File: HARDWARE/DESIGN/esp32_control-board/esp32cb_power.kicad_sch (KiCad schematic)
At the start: 26 parts, among them J301 ESP32m_Prog, U2 LM63615DQDRRRQ1, U3 H7651-33PR, U302 USBLC6-2SC6, U4 AMS1117-3.3

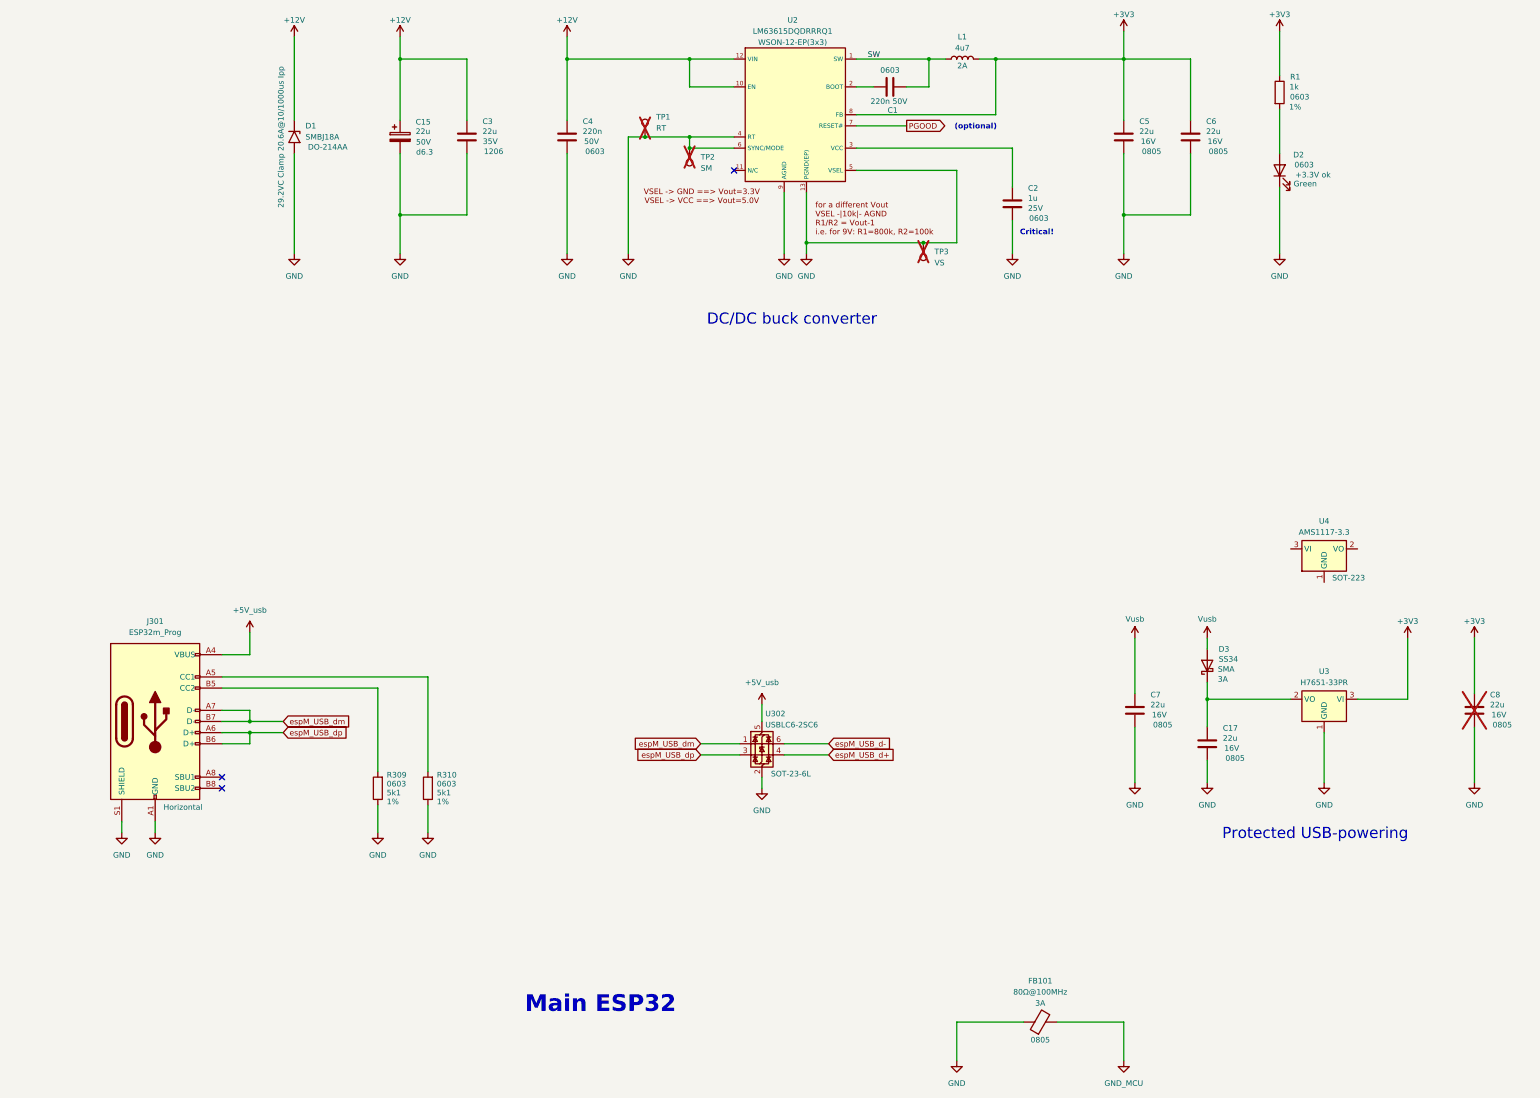
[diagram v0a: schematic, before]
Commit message: 60707 - schematics and readme updated, preliminary PCB-layout prepared
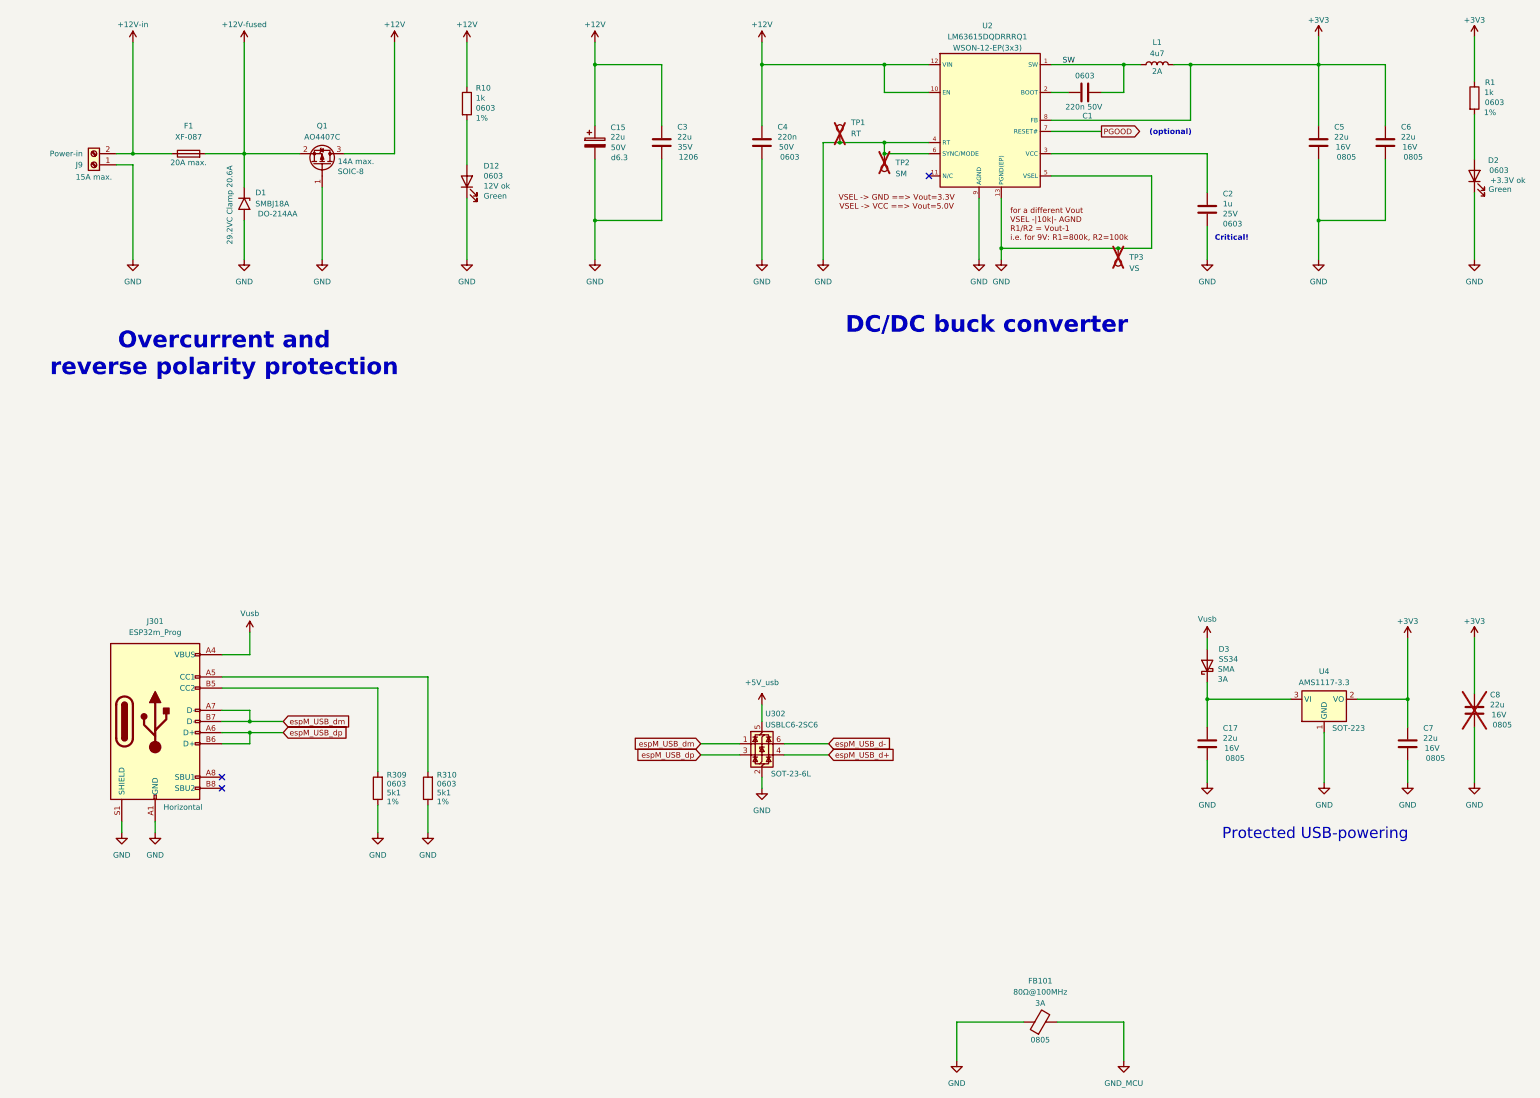
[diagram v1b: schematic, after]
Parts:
- removed U3: H7651-33PR, Package_TO_SOT_SMD:SOT-89-3, symbol Regulator_Linear:AMS1117-3.3
- added D12: 12V ok, LED_SMD:LED_0603_1608Metric, symbol Device:LED
- added F1: XF-087, Fuse:FuseHolder_Blade_ATO_Littelfuse_FLR_178.6165, symbol Device:Fuse
- added J9: Power-in, Connector_AMASS:AMASS_XT30PW-M_1x02_P2.50mm_Horizontal, symbol Connector:Screw_Terminal_01x02
- added Q1: AO4407C, (FOOTPRINTS):SOIC-8_P-MOSFET, symbol Transistor_FET:AO3401A
- added R10: 1k, Resistor_SMD:R_0603_1608Metric, symbol Device:R
- D1: LCSC (none) -> C151256; LCSC part C151256 -> (none); Property 29.2VC Clamp 20.6A@10/1000us Ipp -> 29.2VC Clamp 20.6A
- J301: footprint NICKO:C3151749_USB_TYPE-C_Vertical -> (FOOTPRINTS):C3151749_USB_TYPE-C_Vertical
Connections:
- net +12V: now also Q1.3 (D), R10.1; no longer D1.1 (A1)
- net +3V3: now also C7.1, U4.2 (VO)
- net +5V_usb: no longer J301.A4 (VBUS), J301.A9 (VBUS), J301.B4 (VBUS), J301.B9 (VBUS)
- net GND: now also U4.1 (GND), D12.1 (K), J9.1 (Pin_1), Q1.1 (G)
- net Vusb: now also J301.A4 (VBUS), J301.A9 (VBUS), J301.B4 (VBUS), J301.B9 (VBUS); no longer C7.1
- net at C17.1, D3.1 (K): now also U4.3 (VI)
- new net: D12.2 (A), R10.2
- new net +12V-fused: D1.1 (A1), F1.2, Q1.2 (S)
- new net +12V-in: F1.1, J9.2 (Pin_2)
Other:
- note added: "Overcurrent and reverse polarity protection"
- note removed: "Main ESP32"
- title: (none) -> ESP32-based Control Board
- moved on the sheet: C1, C15, C2, C3, C4, C5, C6, C7, D1, D2, L1, R1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

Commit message: 60710 - schematic and PCB-layout updated
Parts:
- removed J301: ESP32m_Prog, (FOOTPRINTS):C3151749_USB_TYPE-C_Vertical, symbol Connector:USB_C_Receptacle_USB2.0
- removed R10: 1k, Resistor_SMD:R_0603_1608Metric, symbol Device:R
- removed R309, R310: 5k1, Resistor_SMD:R_0603_1608Metric, symbol Device:R
- removed U302: USBLC6-2SC6, Package_TO_SOT_SMD:SOT-23-6, symbol Power_Protection:USBLC6-2SC6
- added C322, C323: 100n, Capacitor_SMD:C_0603_1608Metric, symbol Device:C
- added D14: MMSZ5242B, Diode_SMD:D_SOD-123, symbol Diode:BZX84Cxx
- added Q3: DMP3013SFV-7, Package_SON:Diodes_PowerDI3333-8, symbol Transistor_FET:DMP3013SFV
- added R340: 12k, Resistor_SMD:R_0603_1608Metric, symbol Device:R
- added R343: 5k1, Resistor_SMD:R_0603_1608Metric, symbol Device:R
- Q1: now not fitted; now left out of the parts list
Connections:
- net +12V: now also C322.2, D14.1 (K), Q3.1 (S), Q3.2 (S), Q3.3 (S), R343.2; no longer Q1.3 (D)
- net +12V-fused: now also C323.2, Q3.5 (D); no longer Q1.2 (S)
- net GND: now also C323.1, R340.2; no longer Q1.1 (G)
- net at D12.2 (A): now also R343.1
- new net: C322.1, D14.2 (A), Q3.4 (G), R340.1
- no-connect marks 3 -> 1
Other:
- note added: "Overcurrent and overvoltage protection"
- note added: "Reverse polarity protection"
- note added: "USB-line reverse-current protection"
- note removed: "Overcurrent and reverse polarity protection"
- note removed: "Protected USB-powering"
- moved on the sheet: C1, C15, C17, C2, C3, C4, C5, C6, C7, C8, D1, D12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

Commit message: 60714 - one of two I2C-mux ICs was removed, PCB-layout finished, start tracing
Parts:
- renumbered C15 to C101, C3 to C102, C4 to C103, C323 to C104, C1 to C105, C2 to C106, C322 to C107, C5 to C108, C6 to C109, C17 to C110, C7 to C111, C8 to C112, D1 to D101, D14 to D102, D12 to D103, D2 to D104, D3 to D105, F1 to F101, J9 to J101, L1 to L101, Q1 to Q101, Q3 to Q102, R340 to R101, R343 to R102, R1 to R103, TP1 to TP101, TP2 to TP102, TP3 to TP103, U2 to U101, U4 to U102
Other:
- moved on the sheet: C107, Q101

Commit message: 60825 - Schematic update and PCB-layout started
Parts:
- removed FB101: 80Ω@100MHz, Inductor_SMD:L_0805_2012Metric, symbol Device:FerriteBead
- removed R101: 12k, Resistor_SMD:R_0603_1608Metric, symbol Device:R
- added R108: 12k, Resistor_SMD:R_0603_1608Metric, symbol Device:R
- added R215: 0R, Resistor_SMD:R_0402_1005Metric, symbol Device:R
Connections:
- net GND: now also R108.2, R215.2
- net GND_MCU: now also R215.1
- net at C107.1, D102.2 (A), Q102.4 (G): now also R108.1
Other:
- note added: "Power-GND and Digital GND connection"
- moved on the sheet: C101, C102, C103, C104, C105, C106, C107, C108, C109, C110, C111, C112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

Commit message: 60828 - Schematic updated, preliminary PCB-layout done
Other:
- note added: "Horizontal alternative: C206906"
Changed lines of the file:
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@@
 	(title_block
 		(title "ESP32-based Control Board")
-		(date "2026-08-25")
+		(date "2026-08-28")
 		(rev "2a")
 	)
@@
 		)
 	)
+	(text "Horizontal alternative:\nC206906"
+		(exclude_from_sim no)
+		(at 85.344 57.404 0)
+		(effects
+			(font
+				(size 1.27 1.27)
+			)
+			(justify left)
+		)
+	)

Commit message: 60905 - fuse-holder replaced, led-strip connector added
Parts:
- added F102: XF-087, (FOOTPRINTS):C206906_LittleFuse_01530007Z, symbol Device:Fuse
- F101: Package (none) -> Vertical; now not fitted; now left out of the parts list
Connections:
- net +12V-fused: now also F102.1; no longer F101.2
- net +12V-in: now also J101.1 (Pin_1), F102.2; no longer F101.1, J101.2 (Pin_2)
- net GND: now also J101.2 (Pin_2); no longer J101.1 (Pin_1)
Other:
- note removed: "Horizontal alternative: C206906"
- moved on the sheet: J101

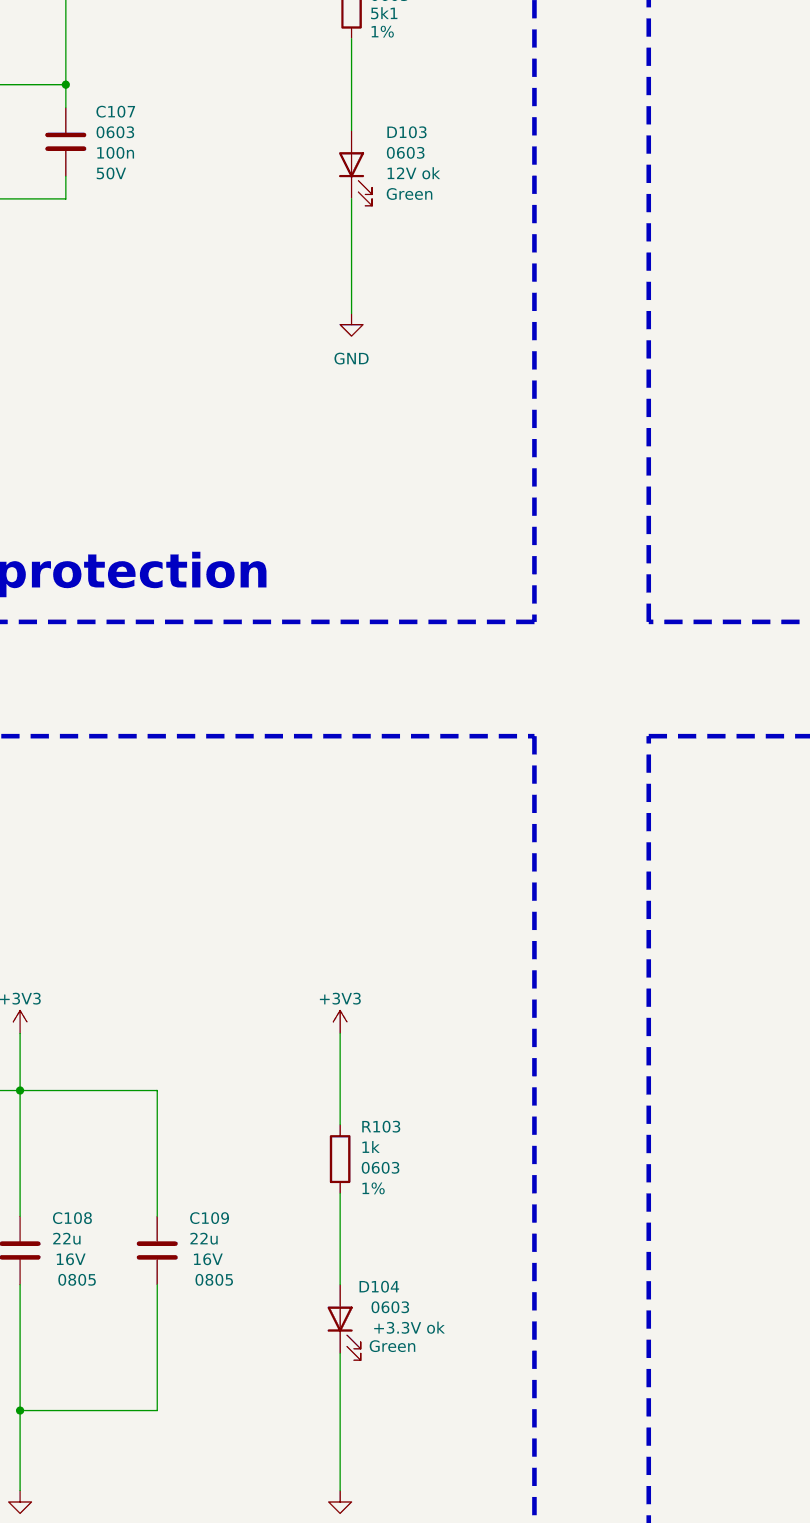
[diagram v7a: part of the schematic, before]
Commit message: 60908 - PCB-layout updated
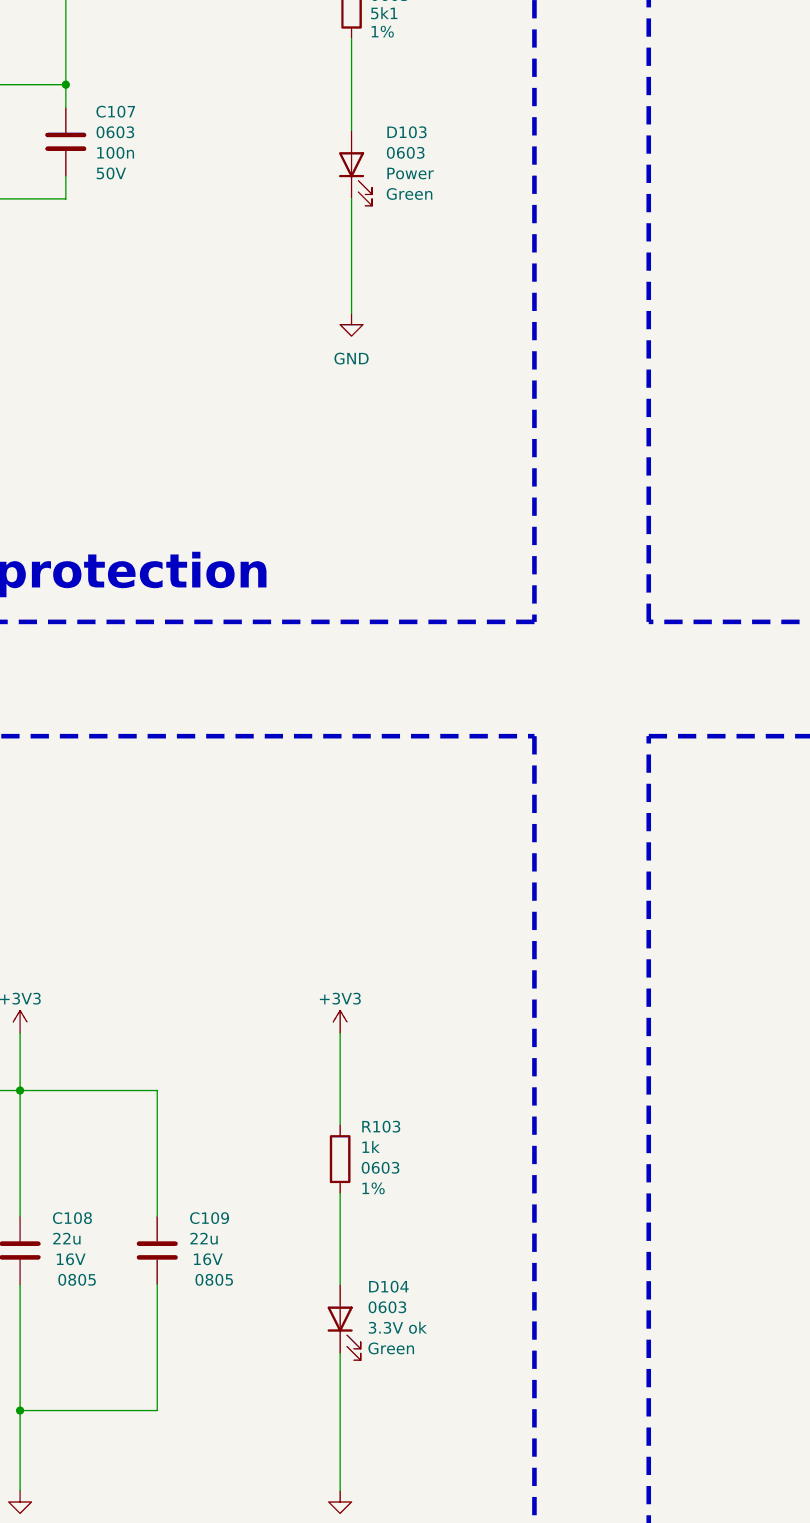
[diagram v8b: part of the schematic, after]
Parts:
- D103: value 12V ok -> Power
- D104: value +3.3V ok -> 3.3V ok
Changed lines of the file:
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@@
 			)
 		)
-		(property "Value" "12V ok"
+		(property "Value" "Power"
 			(at 250.19 77.216 90)
 			(show_name no)
@@
 				)
 				(justify right)
+			)
+		)
+		(property "LCSC" ""
+			(at 246.38 76.2 0)
+			(hide yes)
+			(show_name no)
+			(do_not_autoplace no)
+			(effects
+				(font
+					(size 1.27 1.27)
+				)
 			)
 		)
@@
 		(dnp no)
 		(property "Reference" "D104"
-			(at 249.428 200.914 90)
-			(show_name no)
-			(do_not_autoplace no)
-			(effects
-				(font
-					(size 1.27 1.27)
-				)
-			)
-		)
-		(property "Value" "+3.3V ok"
-			(at 252.73 205.486 90)
-			(show_name no)
-			(do_not_autoplace no)
-			(effects
-				(font
-					(size 1.27 1.27)
-				)
+			(at 248.158 200.914 90)
+			(show_name no)
+			(do_not_autoplace no)
+			(effects
+				(font
+					(size 1.27 1.27)
+				)
+				(justify right)
+			)
+		)
+		(property "Value" "3.3V ok"
+			(at 248.158 205.486 90)
+			(show_name no)
+			(do_not_autoplace no)
+			(effects
+				(font
+					(size 1.27 1.27)
+				)
+				(justify right)
 			)
 		)
@@
 		)
 		(property "Package" "0603"
-			(at 250.698 203.2 90)
-			(show_name no)
-			(do_not_autoplace no)
-			(effects
-				(font
-					(size 1.27 1.27)
-				)
+			(at 248.158 203.2 90)
+			(show_name no)
+			(do_not_autoplace no)
+			(effects
+				(font
+					(size 1.27 1.27)
+				)
+				(justify right)
 			)
 		)
 		(property "Property" "Green"
-			(at 250.952 207.518 90)
-			(show_name no)
-			(do_not_autoplace no)
+			(at 248.158 207.772 90)
+			(show_name no)
+			(do_not_autoplace no)
+			(effects
+				(font
+					(size 1.27 1.27)
+				)
+				(justify right)
+			)
+		)
+		(property "LCSC" ""
+			(at 245.11 204.47 0)
+			(hide yes)
+			(show_name no)
+			(do_not_autoplace no)
